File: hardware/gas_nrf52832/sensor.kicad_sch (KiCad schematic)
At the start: 23 parts, among them IC2 TCK106AG,LF, U3 LPV811DBV, U4 LPV812DGK, U5 BME680

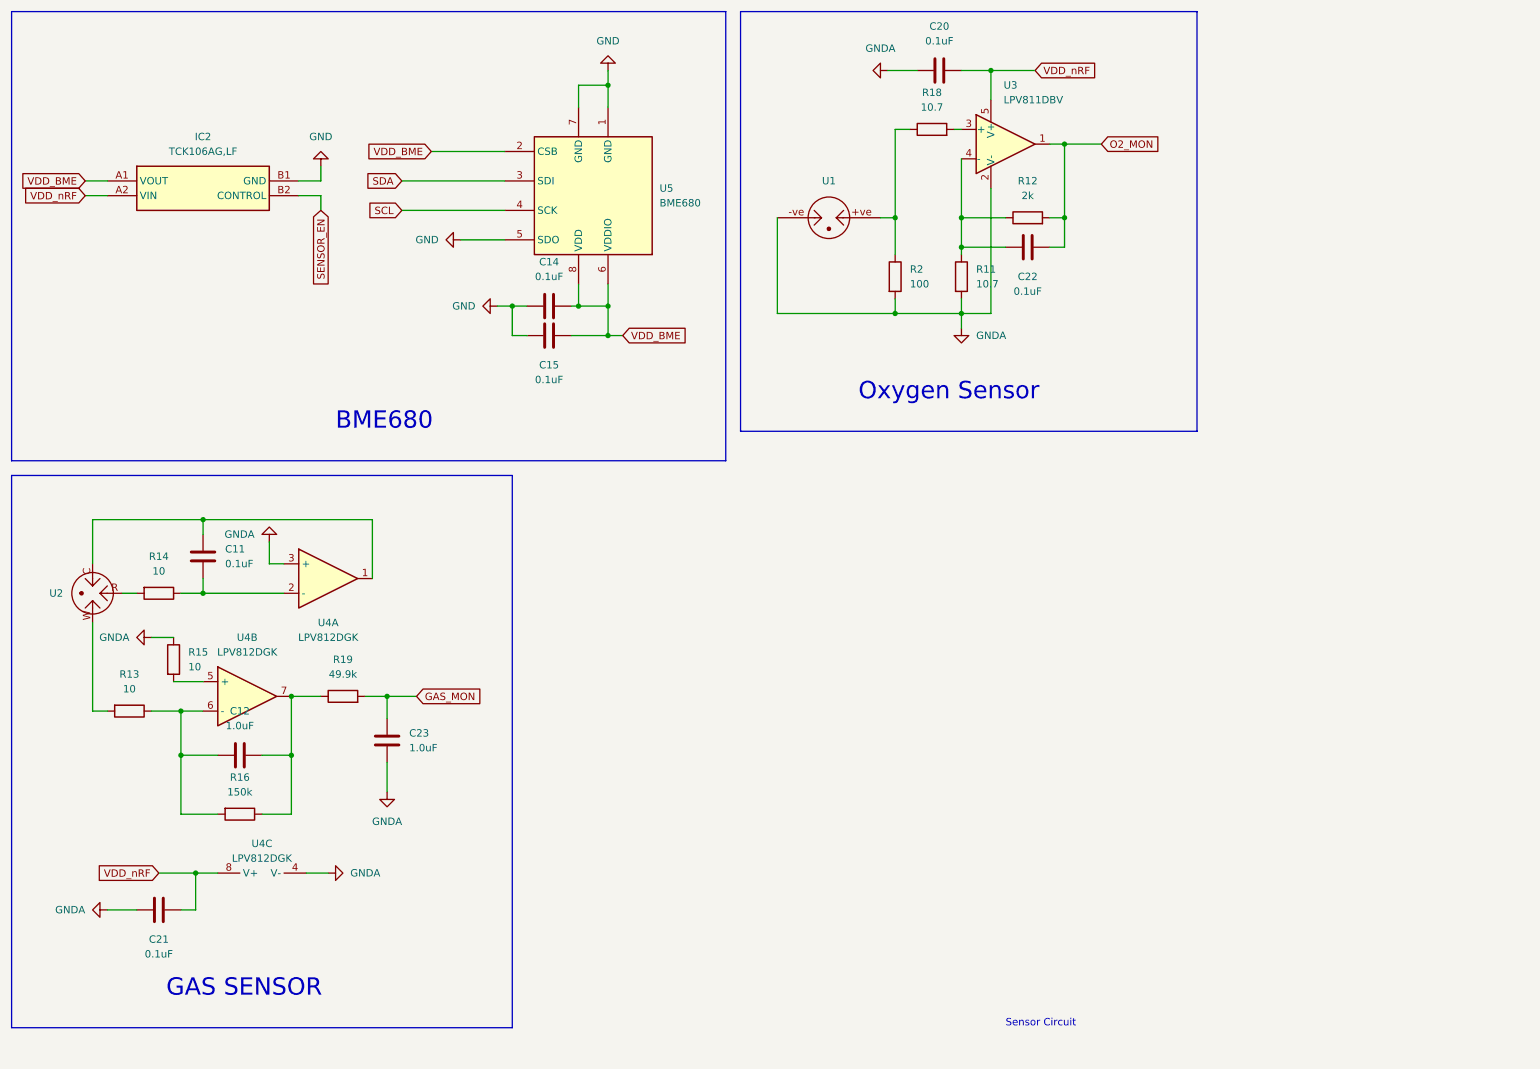
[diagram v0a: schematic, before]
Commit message: hw: fix sensor circuit & fix ERC Error
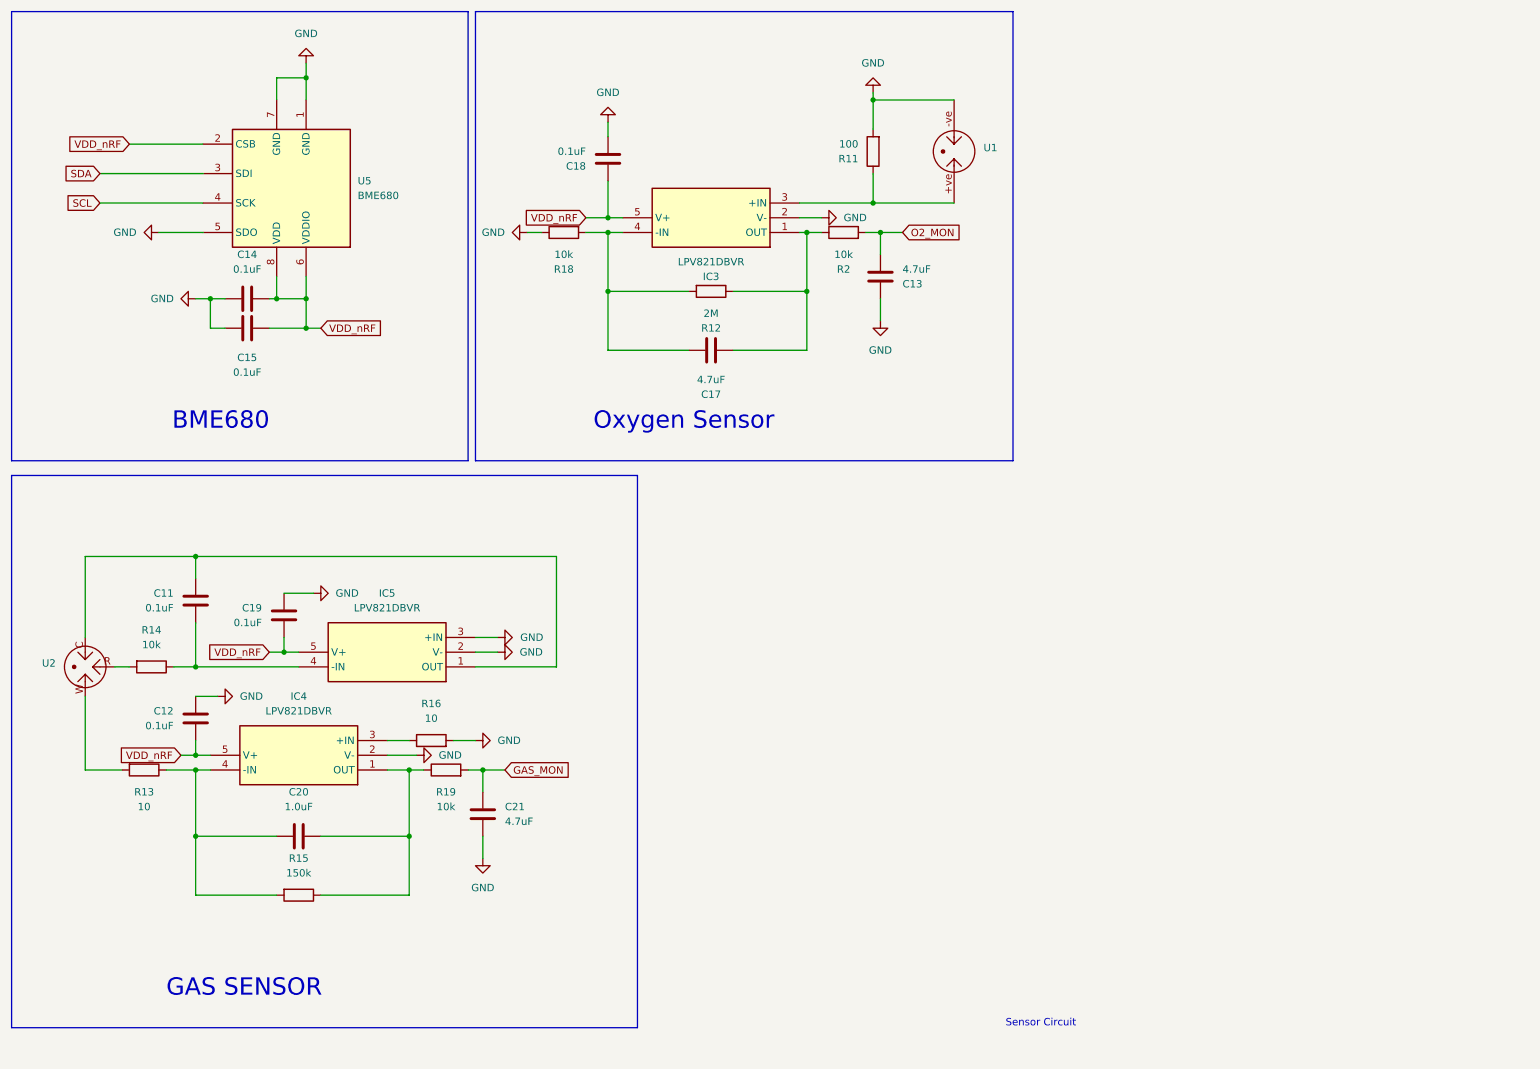
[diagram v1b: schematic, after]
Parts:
- removed C22: 0.1uF, Capacitor_SMD:C_0603_1608Metric, symbol Device:C
- removed C23: 1.0uF, Capacitor_SMD:C_0603_1608Metric, symbol Device:C
- removed IC2: TCK106AG,LF, TCK106AG,LF:BGA4C40P2X2_79X79X59, symbol TCK106AG_LF:TCK106AG,LF
- removed U1: ~, HHS:SS2118_O2, symbol hhs:ss2118_o2
- removed U2: ~, HHS:SS2198_H2S, symbol hhs:ss2198_h2s
- removed U3: LPV811DBV, Package_TO_SOT_SMD:SOT-23-5, symbol Amplifier_Operational:LPV811DBV
- removed U4: LPV812DGK, Package_SO:VSSOP-8_3.0x3.0mm_P0.65mm, symbol Amplifier_Operational:LPV812DGK
- added C13, C17: 4.7uF, Capacitor_SMD:C_0402_1005Metric, symbol Device:C
- added C18, C19: 0.1uF, Capacitor_SMD:C_0402_1005Metric, symbol Device:C
- added IC3, IC4, IC5: LPV821DBVR, LPV821DBVR:SOT95P280X145-5N, symbol LPV821DBVR:LPV821DBVR
- added U1: ~, HHS:SS2118_O2, symbol ss2118_o2:ss2118_o2
- added U2: ~, HHS:SS2198_H2S, symbol ss2198_h2s:ss2198_h2s
- C11, C14, C15: footprint Capacitor_SMD:C_0603_1608Metric -> Capacitor_SMD:C_0402_1005Metric
- C12: value 1.0uF -> 0.1uF; footprint Capacitor_SMD:C_0603_1608Metric -> Capacitor_SMD:C_0402_1005Metric
- C20: value 0.1uF -> 1.0uF; footprint Capacitor_SMD:C_0603_1608Metric -> Capacitor_SMD:C_0402_1005Metric
- C21: value 0.1uF -> 4.7uF; footprint Capacitor_SMD:C_0603_1608Metric -> Capacitor_SMD:C_0402_1005Metric
- R11: value 10.7 -> 100
- R12: value 2k -> 2M
- R14: value 10 -> 10k
- R15: value 10 -> 150k
- R16: value 150k -> 10; footprint Resistor_SMD:R_0603_1608Metric -> Resistor_SMD:R_0402_1005Metric
- R18: value 10.7 -> 10k
- R19: value 49.9k -> 10k
- R2: value 100 -> 10k
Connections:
- net VDD_BME is gone; now on net VDD_nRF: C14.2, C15.2, U5.2 (CSB), U5.6 (VDDIO), U5.8 (VDD)
- net GAS_MON: now also C21.2
- net GND: now also C12.1, C21.1, R11.2, R16.2, R18.1, C13.1, C18.1, C19.1, IC3.2 (V-), IC4.2 (V-), IC5.2 (V-), IC5.3 (+IN), U1.-ve
- net O2_MON: now also R2.2, C13.2; no longer R12.2
- net VDD_nRF: now also C12.2, C18.2, C19.2, IC3.5 (V+), IC4.5 (V+), IC5.5 (V+); no longer C20.2, C21.2
- net at C11.1: now also IC5.1 (OUT), U2.C; no longer R14.1
- net at C11.2: now also R14.1, IC5.4 (-IN)
- net at R15.2: now also C20.2, R13.1, IC4.4 (-IN)
- net at R14.2: now also U2.R
- net at R13.2: now also U2.W
- net at R12.1: now also R2.1, C17.1, IC3.1 (OUT); no longer R11.1
- net at R18.2: now also R12.2, C17.2, IC3.4 (-IN)
- removed net GNDA: C20.1, C21.1, R11.2, R15.1, R2.2
- new net: IC3.3 (+IN), R11.1, U1.+ve
- new net: C20.1, IC4.1 (OUT), R15.1, R19.1
- new net: IC4.3 (+IN), R16.1
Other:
- moved on the sheet: C14, C15, U5

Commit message: feat: hw revision 1.0.2
Rev 1.0.2
- Oxygen Sensor
	- Voltage Amplification Ratio AdjustmentR18(10.7 -> 10k), R12(2.0k -> 2M)
	-> Reduce Current Consumption
	- Addition of lowpass filter for Noise Reduction
- Gas Sensor
	- Addition of lowpass filter for Noise Reduction
- 2 Layter -> 4 Layer
- hansam digitec requirement
	- If USB and RC are very close, errors may occur
	so increase the distance (R1, R23, R24, C22)
- BME680 Sensor Enable ctrl remove
- 32k Crystal Layout fix
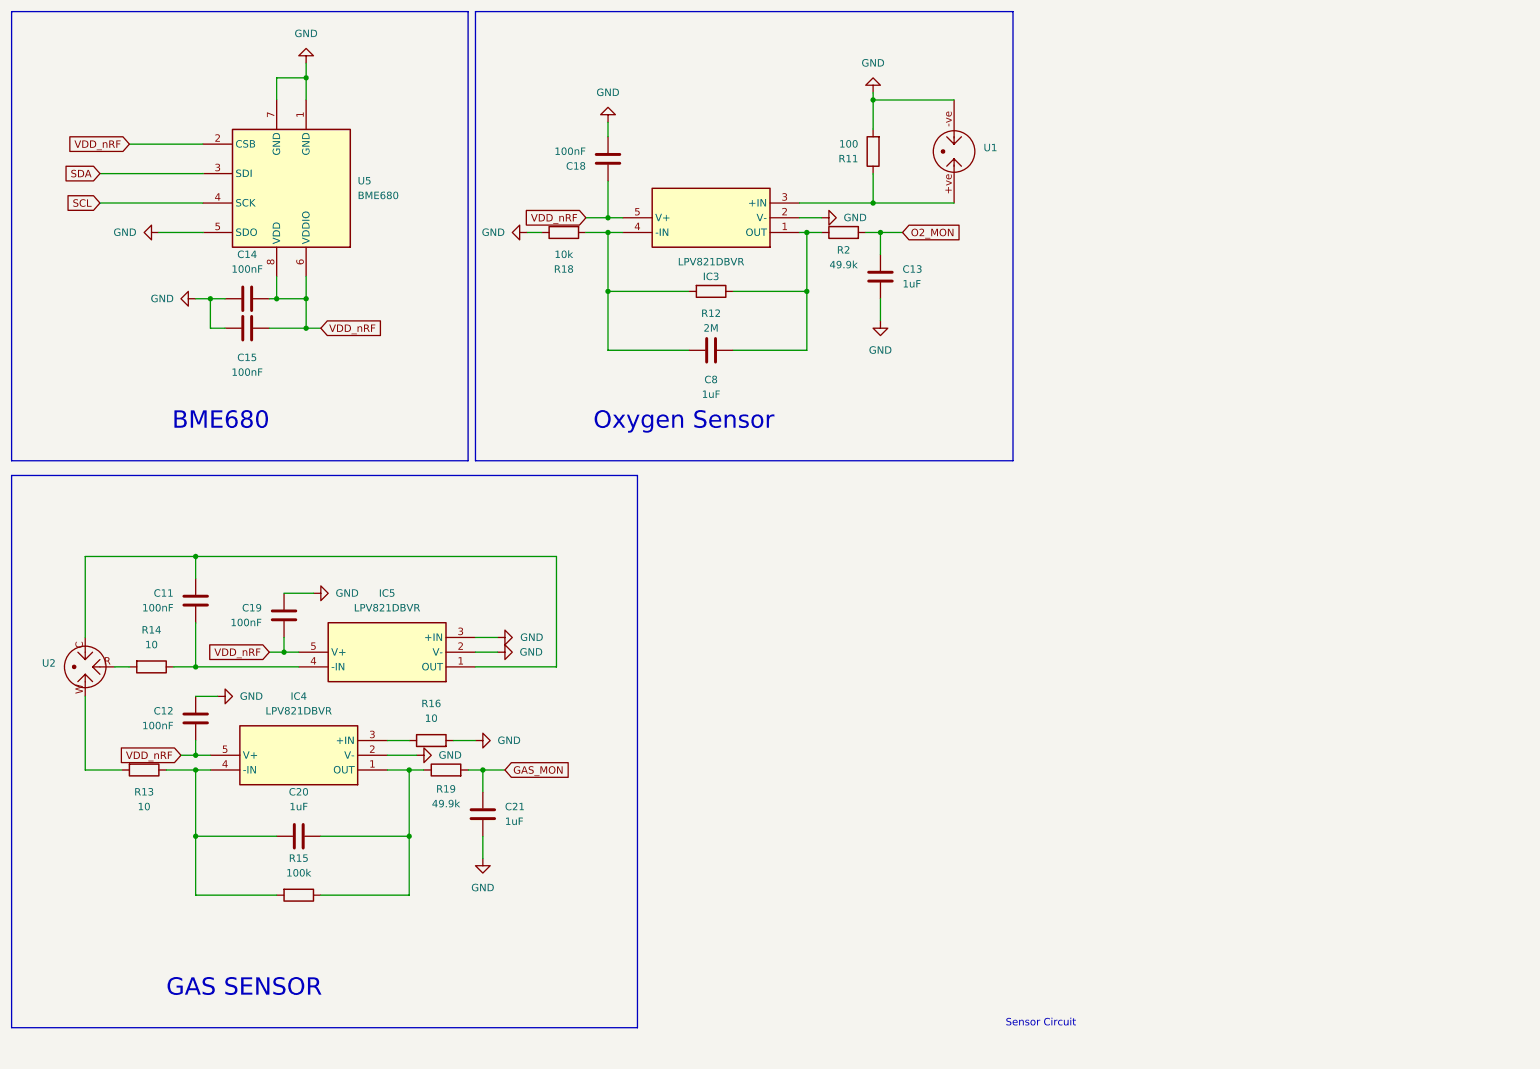
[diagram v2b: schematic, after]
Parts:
- removed C17: 4.7uF, Capacitor_SMD:C_0402_1005Metric, symbol Device:C
- added C8: 1uF, Capacitor_SMD:C_0402_1005Metric, symbol Device:C
- C11, C12, C14, C15, C18, C19: value 0.1uF -> 100nF; MANUFACTURER (none) -> Samsung Electro-Mechanics; Manufacturer_Part_Number (none) -> CL05B104KO5NNNC; Package (none) -> 0402 (1005 Metric); Type (none) -> Surface Mount
- C13, C21: value 4.7uF -> 1uF; MANUFACTURER (none) -> Murata Electronics; Manufacturer_Part_Number (none) -> GRM155C71A105ME11D; Package (none) -> 0402 (1005 Metric); Type (none) -> Surface Mount
- C20: value 1.0uF -> 1uF; MANUFACTURER (none) -> Murata Electronics; Manufacturer_Part_Number (none) -> GRM155C71A105ME11D; Package (none) -> 0402 (1005 Metric); Type (none) -> Surface Mount
- IC3, IC4, IC5: MANUFACTURER (none) -> Texas Instruments; Package (none) -> SOT-23-5; Type (none) -> Surface Mount
- R11: MANUFACTURER (none) -> YAGEO; Manufacturer_Part_Number (none) -> RC0402FR-07100RL; Package (none) -> 0402 (1005 Metric); Type (none) -> Surface Mount
- R12: MANUFACTURER (none) -> YAGEO; Manufacturer_Part_Number (none) -> RC0402FR-072ML; Package (none) -> 0402 (1005 Metric); Type (none) -> Surface Mount
- R13, R16: MANUFACTURER (none) -> YAGEO; Manufacturer_Part_Number (none) -> RC0402FR-0710RL; Package (none) -> 0402 (1005 Metric); Type (none) -> Surface Mount
- R14: value 10k -> 10; MANUFACTURER (none) -> YAGEO; Manufacturer_Part_Number (none) -> RC0402FR-0710RL; Package (none) -> 0402 (1005 Metric); Type (none) -> Surface Mount
- R15: value 150k -> 100k; MANUFACTURER (none) -> YAGEO; Manufacturer_Part_Number (none) -> RC0402FR-07100KL; Package (none) -> 0402 (1005 Metric); Type (none) -> Surface Mount
- R18: MANUFACTURER (none) -> TA-I Tech; Manufacturer_Part_Number (none) -> RM04FTN1002; Package (none) -> 0402 (1005 Metric); Type (none) -> Surface Mount
- R19, R2: value 10k -> 49.9k; MANUFACTURER (none) -> TA-I Tech; Manufacturer_Part_Number (none) -> RM04FTN4992; Package (none) -> 0402 (1005 Metric); Type (none) -> Surface Mount
- U1, U2: now left out of the parts list
- U5: MANUFACTURER (none) -> Bosch Sensortec; Manufacturer_Part_Number (none) -> BME680; Package (none) -> LGA-8; Type (none) -> Surface Mount
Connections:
- net at IC3.1 (OUT), R12.1, R2.1: now also C8.1
- net at IC3.4 (-IN), R12.2, R18.2: now also C8.2

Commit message: test: gas biasing circuit
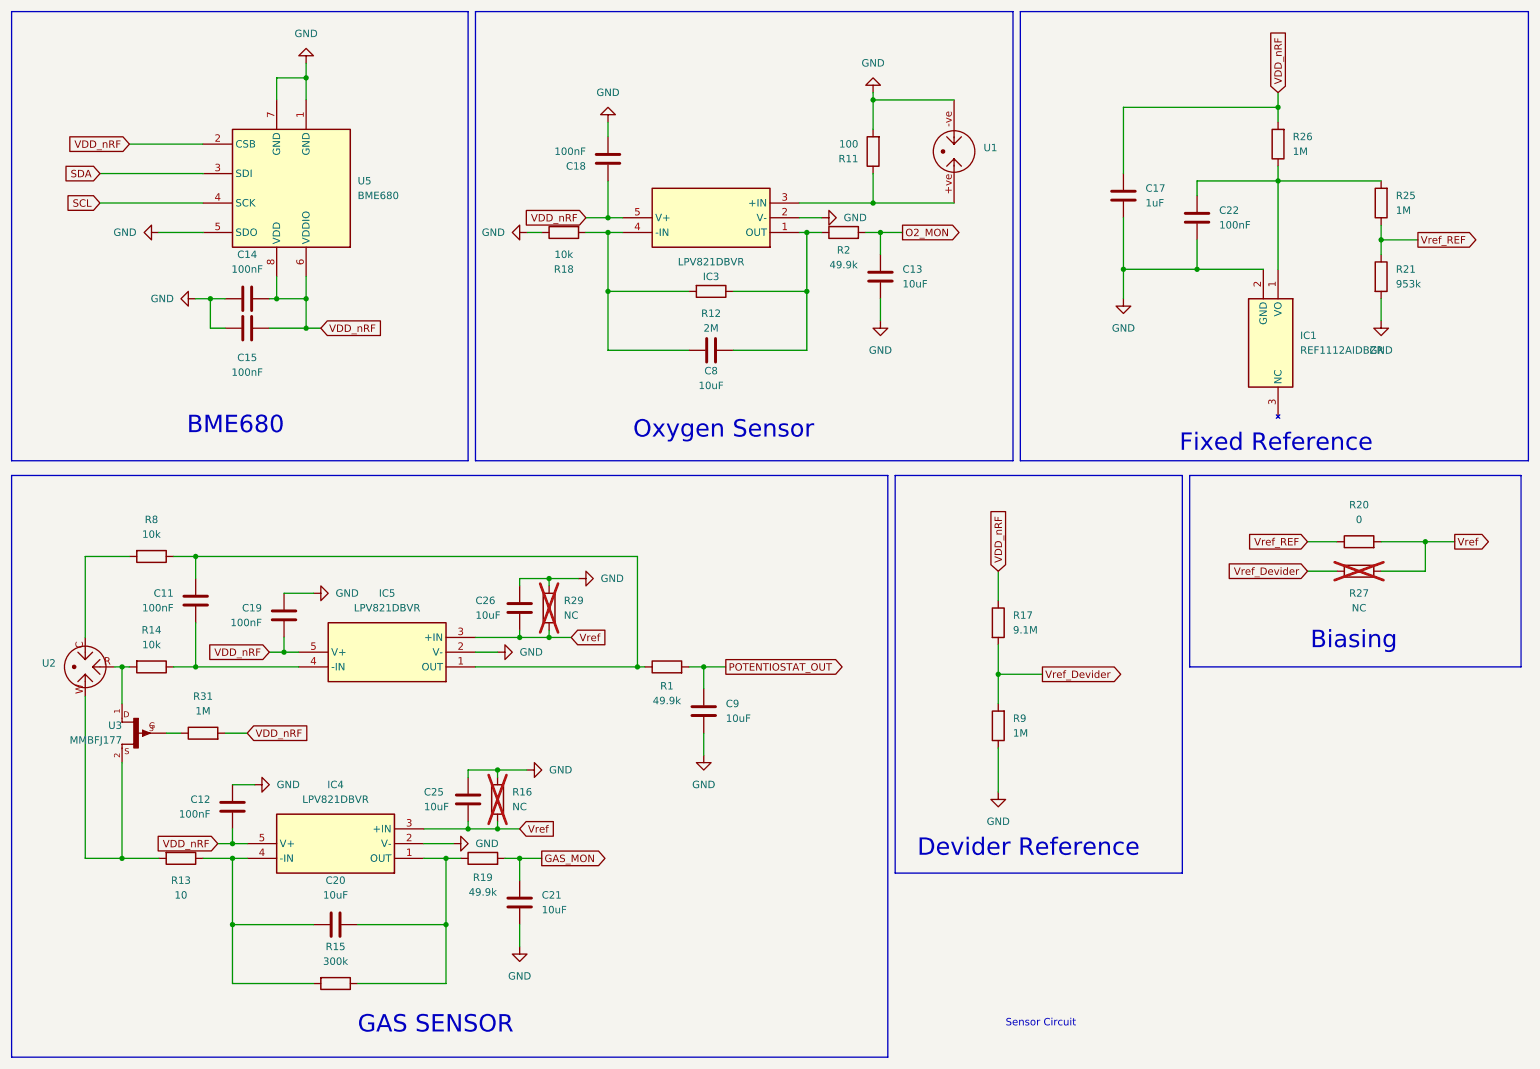
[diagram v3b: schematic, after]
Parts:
- added C17: 1uF, Capacitor_SMD:C_0402_1005Metric, symbol Device:C
- added C22: 100nF, Capacitor_SMD:C_0402_1005Metric, symbol Device:C
- added C25, C26, C9: 10uF, Capacitor_SMD:C_0402_1005Metric, symbol Device:C
- added IC1: REF1112AIDBZR, REF1112AIDBZR:SOT95P237X112-3N, symbol REF1112AIDBZR:REF1112AIDBZR
- added R1: 49.9k, Resistor_SMD:R_0402_1005Metric, symbol Device:R
- added R17: 9.1M, Resistor_SMD:R_0603_1608Metric, symbol Device:R
- added R20: 0, Resistor_SMD:R_0402_1005Metric, symbol Device:R
- added R21: 953k, Resistor_SMD:R_0603_1608Metric, symbol Device:R
- added R25, R26, R31, R9: 1M, Resistor_SMD:R_0402_1005Metric, symbol Device:R
- added R27, R29: NC, Resistor_SMD:R_0402_1005Metric, symbol Device:R
- added R8: 10k, Resistor_SMD:R_0402_1005Metric, symbol Device:R
- added U3: MMBFJ177, MMBFJ177:SOT23, symbol MMBFJ177:MMBFJ177
- C13, C20, C21, C8: value 1uF -> 10uF; Manufacturer_Part_Number GRM155C71A105ME11D -> GRM155C80J106ME11D
- R14: value 10 -> 10k; MANUFACTURER YAGEO -> TA-I Tech; Manufacturer_Part_Number RC0402FR-0710RL -> RM04FTN1002
- R15: value 100k -> 300k; MANUFACTURER YAGEO -> WALSIN; Manufacturer_Part_Number RC0402FR-07100KL -> WR04X3003FTL
- R16: value 10 -> NC; MANUFACTURER YAGEO -> (none); Manufacturer_Part_Number RC0402FR-0710RL -> (none); now not fitted; now left out of the parts list
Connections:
- net GND: now also C17.1, C22.1, C25.2, C26.2, C9.1, IC1.2 (GND), R21.2, R29.2, R9.1; no longer IC5.3 (+IN)
- net VDD_nRF: now also C17.2, R17.1, R26.2, R31.2
- net at C11.1, IC5.1 (OUT): now also R1.1, R8.1; no longer U2.C
- net at R13.2, U2.W: now also U3.2
- net Vref: now reaches IC4.3 (+IN), R16.1
- net Vref: now also IC5.3 (+IN), C25.1, C26.1, R20.2, R27.2, R29.1
- net at R14.2, U2.R: now also U3.1
- new net: C22.2, IC1.1 (VO), R25.2, R26.1
- new net: R8.2, U2.C
- new net: R31.1, U3.3
- new net POTENTIOSTAT_OUT: C9.2, R1.2
- new net Vref_Devider: R17.2, R27.1, R9.2
- new net Vref_REF: R20.1, R21.1, R25.1
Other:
- note added: "Biasing"
- note added: "Devider Reference"
- note added: "Fixed Reference"
- moved on the sheet: C12, C20, C21, IC4, R13, R15, R19

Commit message: feat: hw revision 1.0.4
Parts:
- R21: Manufacturer_Part_Number WR04X9533FTL -> WR06X9533FTL
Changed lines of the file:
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@@
 			)
 		)
-		(property "Manufacturer_Part_Number" "WR04X9533FTL"
+		(property "Manufacturer_Part_Number" "WR06X9533FTL"
 			(at 251.46 60.96 0)
 			(effects
